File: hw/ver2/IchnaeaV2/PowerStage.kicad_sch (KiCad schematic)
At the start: 11 parts, among them Q5 BSS138, U2 LTC7871

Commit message: Trying to optimize the high power loop area
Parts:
- renumbered C7 to C1, C8 to C2, C9 to C3, C10 to C4, C11 to C5, Q5 to Q1, R4 to R1, R8 to R2, R5 to R3, U2 to U1
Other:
- sheet Phase1: file PhaseXDriver.kicad_sch -> Phase1Driver.kicad_sch
- sheet Phase2: file PhaseXDriver.kicad_sch -> Phase2Driver.kicad_sch
- sheet Phase3: file PhaseXDriver.kicad_sch -> Phase3Driver.kicad_sch
- sheet Phase4: file PhaseXDriver.kicad_sch -> Phase4Driver.kicad_sch
- sheet Phase5: file PhaseXDriver.kicad_sch -> Phase5Driver.kicad_sch
- sheet Phase6: file PhaseXDriver.kicad_sch -> Phase6Driver.kicad_sch

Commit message: Trying to further compress power loop area
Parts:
- removed C4: 100nF, Capacitor_SMD:C_0603_1608Metric, symbol Device:C
- added C66, C69, C70: 100nF, Capacitor_SMD:C_0603_1608Metric, symbol Device:C
- added C67, C68: 47pF, Capacitor_SMD:C_0603_1608Metric, symbol Device:C
- added D8, D9: Yellow LED, LED_SMD:LED_0805_2012Metric, symbol Device:LED
- added Q26, Q28, Q29: BSS138, Package_TO_SOT_SMD:SOT-23, symbol Transistor_FET:BSS138
- added Q27: BSS84, Package_TO_SOT_SMD:SOT-23, symbol Transistor_FET:BSS84
- added R28: 22k, Resistor_SMD:R_0603_1608Metric, symbol Device:R_US
- added R29, R36, R37, R38, R40, R43, R44, R45, R46, R50, R51, R53, R55: 10k, Resistor_SMD:R_0603_1608Metric, symbol Device:R_US
- added R30: 30k, Resistor_SMD:R_0603_1608Metric, symbol Device:R_US
- added R31, R35: 470k, Resistor_SMD:R_0603_1608Metric, symbol Device:R_US
- added R32: 15k, Resistor_SMD:R_0603_1608Metric, symbol Device:R_US
- added R33, R39: 787k, Resistor_SMD:R_0603_1608Metric_Pad0.98x0.95mm_HandSolder, symbol Device:R_US
- added R34: 120k, Resistor_SMD:R_0603_1608Metric, symbol Device:R_US
- added R41, R42, R49: 100, Resistor_SMD:R_0603_1608Metric, symbol Device:R_US
- added R47: 3k, Resistor_SMD:R_0603_1608Metric, symbol Device:R_US
- added R48: 1k, Resistor_SMD:R_0603_1608Metric, symbol Device:R_US
- added R52: 68k, Resistor_SMD:R_0603_1608Metric, symbol Device:R_US
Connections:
- net GNDD is gone; now on net GND: Q1.2 (S), R2.1
- net +5P: now also U1.44 (DRVSET), U1.54 (BUCK), R29.2
- net GND: now also U1.16 (SGND), U1.45 (SGND), U1.5 (SGND), U1.65 (SGND), C66.2, C67.2, C68.2, C69.2, C70.2, Q26.2 (S), Q28.2 (S), Q29.2 (S), R28.1, R30.1, R32.1, R36.1, R37.1, R38.1, R40.1, R43.1, R45.1, R50.1, R52.1
- net HT: now also R33.1, R34.1, R39.1
- net VLOW: now also R31.2, R35.1
- net LTC_SS: now reaches U1.1 (SS)
- net LTC_SS: now also C66.1
- net LTC_IMON: now reaches U1.10 (IMON)
- net LTC_SETCUR: now reaches U1.11 (SETCUR)
- net LTC_SETCUR: now also R28.2
- net LTC_OV_HIGH: now reaches U1.13 (OVHigh)
- net LTC_OV_HIGH: now also R33.2, R36.2
- net LTC_UV_HIGH: now reaches U1.14 (UVHigh)
- net LTC_UV_HIGH: now also R34.2, R37.2
- net LTC_OV_LOW: now reaches U1.15 (OVLow)
- net LTC_OV_LOW: now also R35.2, R38.2
- net LTC_RUN: now reaches U1.27 (RUN)
- net LTC_VFB_LOW: now reaches U1.3 (VFBLow)
- net LTC_VFB_LOW: now also R31.1, R32.2
- net PGOOD: now reaches U1.30 (PGOOD)
- net PGOOD: now also D8.1 (K)
- net FAULT: now reaches U1.35 (FAULT)
- net FAULT: now also D9.1 (K)
- net IO_LTC_CSB: now reaches U1.37 (CSB)
- net IO_LTC_SDO: now reaches U1.38 (SDO)
- net IO_LTC_SDI: now reaches U1.39 (SDI)
- net LTC_ITH_LOW: now reaches U1.4 (ITHLow)
- net LTC_ITH_LOW: now also C68.1, R48.2
- net IO_LTC_SCK: now reaches U1.40 (SCLK)
- net LTC_ILIM: now reaches U1.49 (ILM)
- net LTC_ILIM: now also R29.1, R30.2
- net LTC_MODE: now reaches U1.51 (MODE)
- net LTC_MODE: now also Q28.3 (D), R46.2
- net LTC_SYNC: now reaches U1.52 (SYNC)
- net LTC_SYNC: now also Q29.3 (D), R51.1
- net LTC_FREQ: now reaches U1.53 (FREQ)
- net LTC_FREQ: now also R52.2
- net LTC_ITH_HIGH: now reaches U1.6 (ITHHigh)
- net LTC_ITH_HIGH: now also C67.1, R47.2
- net LTC_FB_HIGH: now reaches U1.7 (VFBHigh)
- net LTC_FB_HIGH: now also R39.2, R40.2
- new net: Q26.1 (G), R41.1, R43.2
- new net: Q26.3 (D), Q27.1 (G), R44.1
- new net: D9.2 (A), R53.1
- new net: Q27.3 (D), R46.1
- new net: Q29.1 (G), R49.1, R50.2
- new net: C69.1, R47.1
- new net: Q28.1 (G), R42.1, R45.2
- new net: D8.2 (A), R55.1
- new net: C70.1, R48.1
- new net +5V: Q27.2 (S), R44.2, R51.2, R53.2, R55.2
- new net IO_LTC_CCM: R42.2
- new net IO_LTC_DCCM: R41.2
- new net IO_LTC_SYNC: R49.2
- no-connect marks 0 -> 1
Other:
- note added: "CCM=0, DCM=0: Burst Mode CCM=0, DCM=1: Discontinuous Conduction Mode CCM=1, DCM=0: Forced Continuous Conduction Mode CCM=1, DCM=1: Forced Continuous Conduction Mode"
- note added: "Corresponds to 3/4 * V5, or 40mV peak DCR Sense. With this project's inductor, that's about 25A per phase."
- note added: "Current comparator compensation from LTSpice Sim"
- note added: "Set programmable voltage range from 8.72V-68.88V."
- note added: "Sets max avg inductor current to ~30A. Trimmed with the IDAC_SETCUR register."
- note added: "Soft-Start Time Delay"
- note added: "Spread Spectrum or Ext. Clock"
- note added: "SwitchFreq = R * 8.28kHz/kOhm - 163.5kHz R = 68.1k ~= 400kHz"
- note added: "Voltage References https://www.ti.com/download/kbase/volt/volt_div3.htm FBHigh: Unused OVHigh: 90V UVHigh: 15V OVLow: 56V"

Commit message: Not quite happy with the power stage just yet.
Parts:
- C1: value 10uF -> 10uF-25V; Voltage (none) -> 25
- C3: value 10uF -> 10uF-25V
- C5: value 10uF-75V -> 10uF-100v; LCSC N/A -> C576517
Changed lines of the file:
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@@
 			)
 		)
-		(property "Value" "10uF"
+		(property "Value" "10uF-25V"
 			(at 109.22 33.0199 0)
 			(effects
@@
 			)
 		)
-		(property "Value" "10uF-75V"
+		(property "Value" "10uF-100v"
 			(at 177.8 36.8299 0)
 			(effects
@@
 			)
 		)
-		(property "LCSC" "N/A"
+		(property "LCSC" "C576517"
 			(at 173.99 35.56 0)
 			(effects
@@
 			)
 		)
-		(property "Value" "10uF"
+		(property "Value" "10uF-25V"
 			(at 71.12 33.0199 0)
 			(effects
@@
 			)
 		)
-		(property "Field-1" ""
+		(property "Voltage" "25"
 			(at 67.31 31.75 0)
 			(effects

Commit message: Sync work to main PC
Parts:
- removed D1: SS210, Diode_SMD:D_SMA, symbol Device:D_Schottky
- added C74, C78, C79, C80, C81: 10uF, Capacitor_SMD:C_0603_1608Metric, symbol Device:C
- added C75: 4.7uF, Capacitor_SMD:C_0603_1608Metric, symbol Device:C
- added C76: 100nF, Capacitor_SMD:C_0603_1608Metric, symbol Device:C
- added C77: 47pF, Capacitor_SMD:C_0603_1608Metric, symbol Device:C
- added D1: SB10100L, Package_TO_SOT_SMD:TO-277A, symbol Device:D_Schottky_AAK
- added D10: PMEG10010ELRX, Diode_SMD:D_SOD-123, symbol Device:D_Schottky
- added L7: 22uH, Inductors:TYS5020220M, symbol Device:L_Ferrite
- added R57: 68k, Resistor_SMD:R_0603_1608Metric, symbol Device:R_US
- added R58: 510k, Resistor_SMD:R_0603_1608Metric, symbol Device:R_US
- added R59: 7.5k, Resistor_SMD:R_0603_1608Metric, symbol Device:R_US
- added R60: 100k, Resistor_SMD:R_0603_1608Metric, symbol Device:R_US
- added U8: AP66200FVBW-13, Package_DFN_QFN:QFN-16-1EP_4x4mm_P0.65mm_EP2.5x2.5mm, symbol ap66200:AP66200FVBW
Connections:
- net DRVcc: now also D10.2 (A)
- net GND: now also C74.2, C75.2, C78.2, C79.2, C80.2, C81.2, R57.2, R59.2, U8.12 (MSYNC), U8.16 (GND), U8.17 (EPAD), U8.8 (PGND), U8.9 (PGND)
- net VLOW: now also D1.1 (A), D1.2 (A)
- net at C5.1, U1.42 (EXTVcc): now also C74.1, D1.3 (K), R57.1, R58.1, U8.3 (VIN), U8.4 (VIN)
- new net: C76.2, L7.1, U8.6 (SW), U8.7 (SW)
- new net: R58.2, U8.10 (EN)
- new net: C77.1, R59.1, R60.1, U8.15 (FB)
- new net: C76.1, U8.5 (BOOST)
- new net +12V: C77.2, C78.1, C79.1, C80.1, C81.1, D10.1 (K), L7.2, R60.2
- new net AP_VCC: C75.1, U8.11 (FS), U8.14 (SS), U8.2 (VCC)
- new net VOUT_LV: U8.1 (BIAS)
- no-connect marks 1 -> 2
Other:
- removed sheet GateDriverSupply
- note added: "AP66300 Drop In Replacement"
- note added: "Fig.40, sets UVLO ~12v."
- note added: "Select between the current limited +VSW output of the LTC7871 and the high power rail."

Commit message: More power stage layout
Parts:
- removed C2: 100nF, Capacitor_SMD:C_0603_1608Metric, symbol Device:C
- removed D8, D9: Yellow LED, LED_SMD:LED_0805_2012Metric, symbol Device:LED
- removed R53, R55: 10k, Resistor_SMD:R_0603_1608Metric, symbol Device:R_US
- added TP1, TP14, TP15, TP2, TP3, TP4, TP5: TestPoint, TestPoint:TestPoint_Pad_D1.0mm, symbol Connector:TestPoint
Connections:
- net GND: now also TP5.1
- net IO_LTC_CSB: now also TP4.1
- net IO_LTC_SCK: now also TP1.1
- net IO_LTC_SDI: now also TP2.1
- net IO_LTC_SDO: now also TP3.1
- net Phase1/PWMEN: now also TP15.1
- net at Q1.1 (G), R2.2, R3.1: now also TP14.1
- net IO_LTC_PWM_EN: now reaches R3.2
- net FAULT: no longer names the net of U1.35 (FAULT)
- net PGOOD: no longer names the net of U1.30 (PGOOD)
- no-connect marks 2 -> 4
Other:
- moved on the sheet: C1

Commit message: Sync
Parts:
- removed C74: 10uF, Capacitor_SMD:C_0603_1608Metric, symbol Device:C
- added C2: 10uF-100v, Capacitor_SMD:C_1210_3225Metric_Pad1.33x2.70mm_HandSolder, symbol Device:C
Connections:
- net VOUT_LV is gone; now on net +12V: U8.1 (BIAS)
- net GND: now also C2.2
- net at C5.1, D1.3 (K), R57.1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: now also C2.1
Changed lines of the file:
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@@
 		)
 	)
-	(hierarchical_label "VOUT_LV"
-		(shape output)
-		(at 274.32 48.26 180)
-		(fields_autoplaced yes)
-		(effects
-			(font
-				(size 1.27 1.27)
-			)
-			(justify right)
-		)
-	)
 	(hierarchical_label "IO_LTC_CCM"
 		(shape input)
@@
 	(symbol
 		(lib_id "Device:C")
-		(at 243.84 45.72 0)
-		(unit 1)
-		(exclude_from_sim no)
-		(in_bom yes)
-		(on_board yes)
-		(dnp no)
-		(fields_autoplaced yes)
-		(property "Reference" "C74"
-			(at 247.65 44.4499 0)
-			(effects
-				(font
-					(size 1.27 1.27)
-				)
-				(justify left)
-			)
-		)
-		(property "Value" "10uF"
-			(at 247.65 46.9899 0)
-			(effects
-				(font
-					(size 1.27 1.27)
-				)
-				(justify left)
-			)
-		)
-		(property "Footprint" "Capacitor_SMD:C_0603_1608Metric"
-			(at 244.8052 49.53 0)
-			(effects
-				(font
-					(size 1.27 1.27)
-				)
-				(hide yes)
-			)
-		)
-		(property "Datasheet" "~"
-			(at 243.84 45.72 0)
-			(effects
-				(font
-					(size 1.27 1.27)
-				)
-				(hide yes)
-			)
-		)
-		(property "Description" "Unpolarized capacitor"
-			(at 243.84 45.72 0)
-			(effects
-				(font
-					(size 1.27 1.27)
-				)
-				(hide yes)
-			)
-		)
-		(property "Field-1" ""
-			(at 243.84 45.72 0)
-			(effects
-				(font
-					(size 1.27 1.27)
-				)
-				(hide yes)
-			)
-		)
-		(property "Digikey" "N/A"
-			(at 243.84 45.72 0)
-			(effects
-				(font
-					(size 1.27 1.27)
-				)
-				(hide yes)
-			)
-		)
-		(property "LCSC" "C96446"
-			(at 243.84 45.72 0)
-			(effects
-				(font
-					(size 1.27 1.27)
-				)
-				(hide yes)
-			)
-		)
-		(pin "1"
-		)
-		(pin "2"
-		)
-		(instances
-			(project "IchnaeaV2"
-				(path "/93408532-1ffa-463d-873c-16289d2b7987/31a930eb-86fc-490d-aa2b-31b72c4dd29d"
-					(reference "C74")
-					(unit 1)
-				)
-			)
-		)
-	)
-	(symbol
-		(lib_id "Device:C")
 		(at 105.41 31.75 0)
 		(unit 1)
@@
 	)
 	(symbol
+		(lib_id "Device:C")
+		(at 243.84 45.72 0)
+		(unit 1)
+		(exclude_from_sim no)
+		(in_bom yes)
+		(on_board yes)
+		(dnp no)
+		(fields_autoplaced yes)
+		(property "Reference" "C2"
+			(at 247.65 44.4499 0)
+			(effects
+				(font
+					(size 1.27 1.27)
+				)
+				(justify left)
+			)
+		)
+		(property "Value" "10uF-100v"
+			(at 247.65 46.9899 0)
+			(effects
+				(font
+					(size 1.27 1.27)
+				)
+				(justify left)
+			)
+		)
+		(property "Footprint" "Capacitor_SMD:C_1210_3225Metric_Pad1.33x2.70mm_HandSolder"
+			(at 244.8052 49.53 0)
+			(effects
+				(font
+					(size 1.27 1.27)
+				)
+				(hide yes)
+			)
+		)
+		(property "Datasheet" "~"
+			(at 243.84 45.72 0)
+			(effects
+				(font
+					(size 1.27 1.27)
+				)
+				(hide yes)
+			)
+		)
+		(property "Description" "Unpolarized capacitor"
+			(at 243.84 45.72 0)
+			(effects
+				(font
+					(size 1.27 1.27)
+				)
+				(hide yes)
+			)
+		)
+		(property "Field-1" ""
+			(at 243.84 45.72 0)
+			(effects
+				(font
+					(size 1.27 1.27)
+				)
+				(hide yes)
+			)
+		)
+		(property "Digikey" "445-CGA6P1X7R1N106M250ACCT-ND"
+			(at 243.84 45.72 0)
+			(effects
+				(font
+					(size 1.27 1.27)
+				)
+				(hide yes)
+			)
+		)
+		(property "LCSC" "C576517"
+			(at 243.84 45.72 0)
+			(effects
+				(font
+					(size 1.27 1.27)
+				)
+				(hide yes)
+			)
+		)
+		(pin "1"
+		)
+		(pin "2"
+		)
+		(instances
+			(project "IchnaeaV2"
+				(path "/93408532-1ffa-463d-873c-16289d2b7987/31a930eb-86fc-490d-aa2b-31b72c4dd29d"
+					(reference "C2")
+					(unit 1)
+				)
+			)
+		)
+	)
+	(symbol
 		(lib_id "power:GND")
 		(at 243.84 49.53 0)
@@
 					(unit 1)
 				)
+			)
+		)
+	)
+	(symbol
+		(lib_id "power:+12V")
+		(at 274.32 48.26 90)
+		(unit 1)
+		(exclude_from_sim no)
+		(in_bom yes)
+		(on_board yes)
+		(dnp no)
+		(fields_autoplaced yes)
+		(property "Reference" "#PWR010"
+			(at 278.13 48.26 0)
+			(effects
+				(font
+					(size 1.27 1.27)
+				)
+				(hide yes)
+			)
+		)
+		(property "Value" "+12V"
+			(at 270.51 48.2599 90)
+			(effects
+				(font
+					(size 1.27 1.27)
+				)
+				(justify left)
+			)
+		)
+		(property "Footprint" ""
+			(at 274.32 48.26 0)
+			(effects
+				(font
+					(size 1.27 1.27)
+				)
+				(hide yes)
+			)
+		)
+		(property "Datasheet" ""
+			(at 274.32 48.26 0)
+			(effects
+				(font
+					(size 1.27 1.27)
+				)
+				(hide yes)
+			)
+		)
+		(property "Description" "Power symbol creates a global label with name \"+12V\""
+			(at 274.32 48.26 0)
+			(effects
+				(font
+					(size 1.27 1.27)
+				)
+				(hide yes)
+			)
+		)
+		(pin "1"
+		)
+		(instances
+			(project "IchnaeaV2"
+				(path "/93408532-1ffa-463d-873c-16289d2b7987/31a930eb-86fc-490d-aa2b-31b72c4dd29d"
+					(reference "#PWR010")
+					(unit 1)
+				)

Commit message: Partially work through the V1 notes. Start adding some of the control stage circuitry.
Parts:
- removed Q26, Q28, Q29: BSS138, Package_TO_SOT_SMD:SOT-23, symbol Transistor_FET:BSS138
- removed Q27: BSS84, Package_TO_SOT_SMD:SOT-23, symbol Transistor_FET:BSS84
- removed R41, R42, R49: 100, Resistor_SMD:R_0603_1608Metric, symbol Device:R_US
- removed R43, R44, R45, R46, R50, R51: 10k, Resistor_SMD:R_0603_1608Metric, symbol Device:R_US
- added R106, R94: 6.2k-0.25w, Resistor_SMD:R_1206_3216Metric_Pad1.30x1.75mm_HandSolder, symbol Device:R_US
- added R93: 470k, Resistor_SMD:R_0603_1608Metric, symbol Device:R_US
- added TP16, TP17, TP18, TP55, TP56, TP57, TP58, TP59, TP60, TP61, TP62, TP63: TestPoint, TestPoint:TestPoint_Pad_D1.0mm, symbol Connector:TestPoint
- C75: value 4.7uF -> 10uF-25V; LCSC C19666 -> C96446
- C78, C79, C80, C81: value 10uF -> 10uF-25V
- L7: footprint Inductors:TYS5020220M -> Inductor_SMD:L_Wuerth_HCI-1040; Digikey 240-2706-1-ND -> N/A; LCSC N/A -> C182173
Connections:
- net LTC_SYNC is gone; now on net IO_LTC_SYNC: U1.52 (SYNC)
- net +12V: now also TP16.1
- net GND: now also R106.1, R93.1, R94.1, TP17.1
- net HT: now also R106.2
- net IO_LTC_SYNC: now also TP55.1
- net LTC_OV_HIGH: now also TP62.1
- net LTC_OV_LOW: now also TP60.1
- net LTC_SETCUR: now also TP59.1
- net LTC_SS: now also R93.2, TP58.1
- net LTC_UV_HIGH: now also TP61.1
- net LTC_VFB_LOW: now also TP63.1
- net VLOW: now also R94.2
- net at C2.1, C5.1, D1.3 (K)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: now also TP18.1
- net LTC_IMON renamed IO_LTC_IMON
- net LTC_MODE renamed IO_LTC_MODE
- net IO_LTC_MODE: now also TP57.1
- net LTC_RUN renamed IO_LTC_RUN
- net IO_LTC_RUN: now also TP56.1
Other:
- note added: "Bleeder Resistors"
- note removed: "CCM=0, DCM=0: Burst Mode CCM=0, DCM=1: Discontinuous Conduction Mode CCM=1, DCM=0: Forced Continuous Conduction Mode CCM=1, DCM=1: Forced Continuous Conduction Mode"
- note removed: "Spread Spectrum or Ext. Clock"
- moved on the sheet: C1, C2, C3, C5, C66, C67, C68, C69, C70, C75, C76, C77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

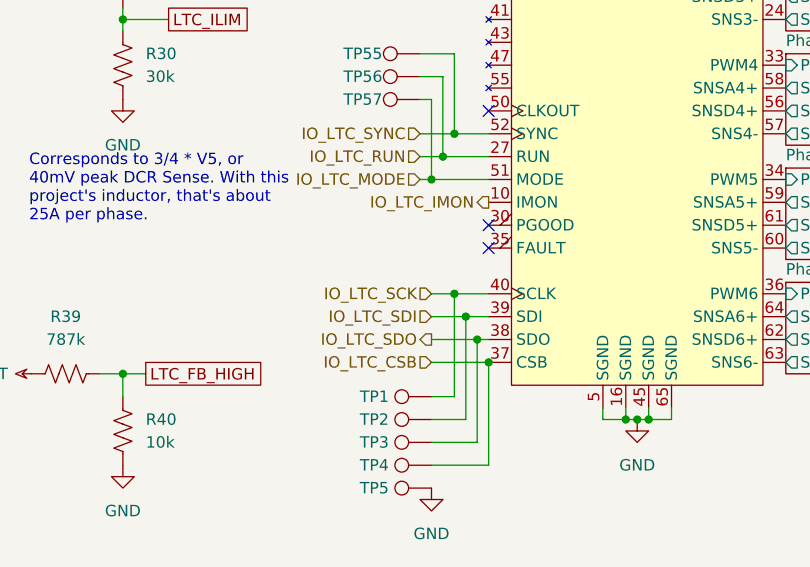
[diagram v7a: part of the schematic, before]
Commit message: Partial pin mapping. ESD protection on signals that exit the board.
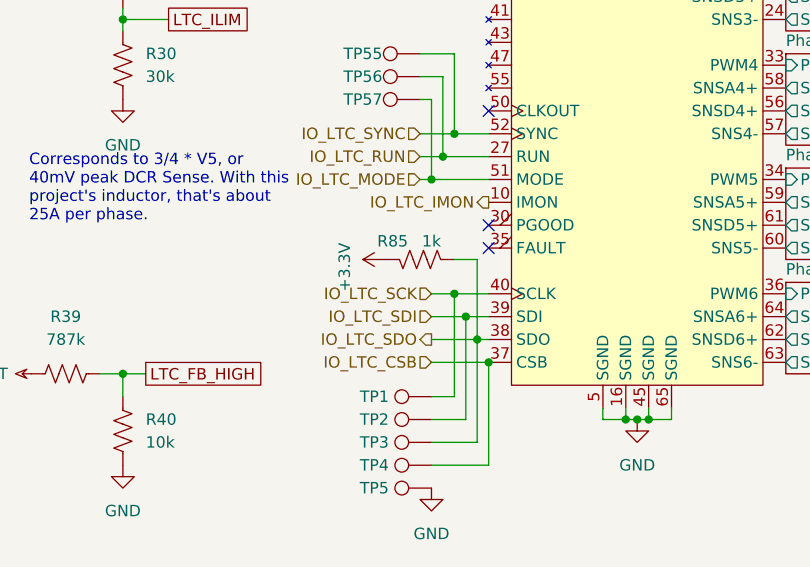
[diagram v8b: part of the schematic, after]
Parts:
- added R85: 1k, Resistor_SMD:R_0603_1608Metric, symbol Device:R_US
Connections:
- net IO_LTC_SDO: now also R85.1
- new net +3.3V: R85.2
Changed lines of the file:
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@@
 	(wire
 		(pts
+			(xy 186.69 163.83) (xy 189.23 163.83)
+		)
+		(stroke
+			(width 0)
+			(type default)
+		)
+	)
+	(wire
+		(pts
 			(xy 182.88 146.05) (xy 184.15 146.05)
 		)
@@
 	(wire
 		(pts
+			(xy 189.23 163.83) (xy 189.23 172.72)
+		)
+		(stroke
+			(width 0)
+			(type default)
+		)
+	)
+	(wire
+		(pts
 			(xy 355.6 78.74) (xy 355.6 80.01)
 		)
@@
 	(symbol
 		(lib_id "Device:R_US")
+		(at 182.88 163.83 270)
+		(mirror x)
+		(unit 1)
+		(exclude_from_sim no)
+		(in_bom yes)
+		(on_board yes)
+		(dnp no)
+		(property "Reference" "R85"
+			(at 179.832 161.798 90)
+			(effects
+				(font
+					(size 1.27 1.27)
+				)
+			)
+		)
+		(property "Value" "1k"
+			(at 184.15 161.798 90)
+			(effects
+				(font
+					(size 1.27 1.27)
+				)
+			)
+		)
+		(property "Footprint" "Resistor_SMD:R_0603_1608Metric"
+			(at 182.626 162.814 90)
+			(effects
+				(font
+					(size 1.27 1.27)
+				)
+				(hide yes)
+			)
+		)
+		(property "Datasheet" "~"
+			(at 182.88 163.83 0)
+			(effects
+				(font
+					(size 1.27 1.27)
+				)
+				(hide yes)
+			)
+		)
+		(property "Description" "Resistor, US symbol"
+			(at 182.88 163.83 0)
+			(effects
+				(font
+					(size 1.27 1.27)
+				)
+				(hide yes)
+			)
+		)
+		(property "Field-1" ""
+			(at 182.88 163.83 0)
+			(effects
+				(font
+					(size 1.27 1.27)
+				)
+				(hide yes)
+			)
+		)
+		(property "Digikey" "N/A"
+			(at 182.88 163.83 0)
+			(effects
+				(font
+					(size 1.27 1.27)
+				)
+				(hide yes)
+			)
+		)
+		(property "LCSC" "C21190"
+			(at 182.88 163.83 0)
+			(effects
+				(font
+					(size 1.27 1.27)
+				)
+				(hide yes)
+			)
+		)
+		(pin "1"
+		)
+		(pin "2"
+		)
+		(instances
+			(project "IchnaeaV2"
+				(path "/93408532-1ffa-463d-873c-16289d2b7987/31a930eb-86fc-490d-aa2b-31b72c4dd29d"
+					(reference "R85")
+					(unit 1)
+				)
+			)
+		)
+	)
+	(symbol
+		(lib_id "Device:R_US")
 		(at 111.76 142.24 180)
 		(unit 1)
@@
 					(unit 1)
 				)
+			)
+		)
+	)
+	(symbol
+		(lib_id "power:+3.3VP")
+		(at 179.07 163.83 90)
+		(unit 1)
+		(exclude_from_sim no)
+		(in_bom yes)
+		(on_board yes)
+		(dnp no)
+		(property "Reference" "#PWR0151"
+			(at 180.34 160.02 0)
+			(effects
+				(font
+					(size 1.27 1.27)
+				)
+				(hide yes)
+			)
+		)
+		(property "Value" "+3.3V"
+			(at 174.498 167.386 0)
+			(effects
+				(font
+					(size 1.27 1.27)
+				)
+				(justify left)
+			)
+		)
+		(property "Footprint" ""
+			(at 179.07 163.83 0)
+			(effects
+				(font
+					(size 1.27 1.27)
+				)
+				(hide yes)
+			)
+		)
+		(property "Datasheet" ""
+			(at 179.07 163.83 0)
+			(effects
+				(font
+					(size 1.27 1.27)
+				)
+				(hide yes)
+			)
+		)
+		(property "Description" "Power symbol creates a global label with name \"+3.3VP\""
+			(at 179.07 163.83 0)
+			(effects
+				(font
+					(size 1.27 1.27)
+				)
+				(hide yes)
+			)
+		)
+		(pin "1"
+		)
+		(instances
+			(project "IchnaeaV2"
+				(path "/93408532-1ffa-463d-873c-16289d2b7987/31a930eb-86fc-490d-aa2b-31b72c4dd29d"
+					(reference "#PWR0151")
+					(unit 1)
+				)
